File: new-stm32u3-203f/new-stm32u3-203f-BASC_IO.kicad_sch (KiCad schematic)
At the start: 0 parts

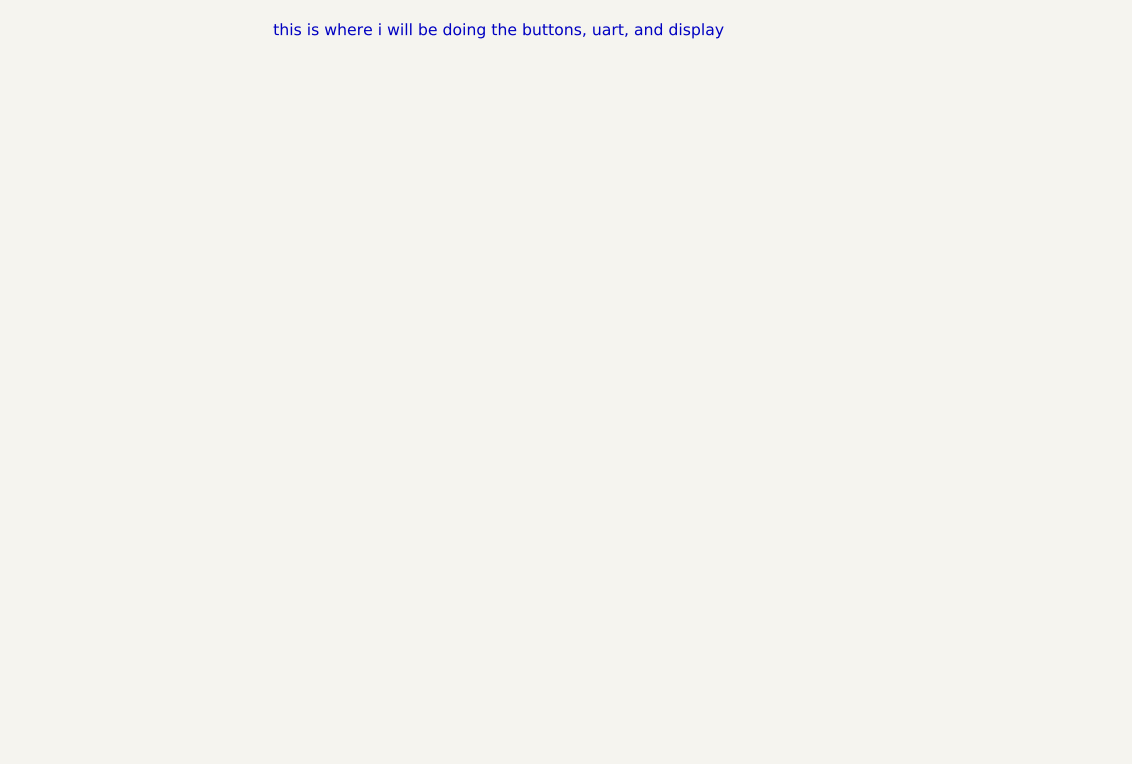
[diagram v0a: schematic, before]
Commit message: added buttons, added uart, added display.
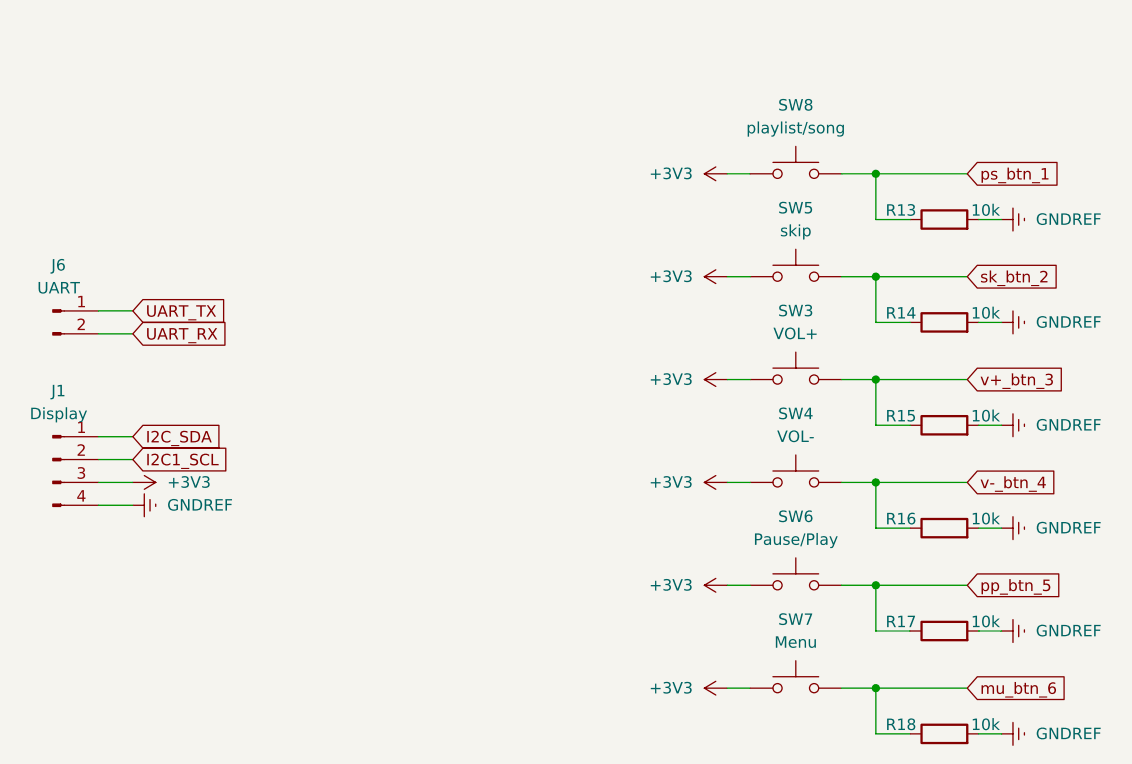
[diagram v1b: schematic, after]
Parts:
- added J1: Display, symbol Connector:Conn_01x04_Pin
- added J6: UART, symbol Connector:Conn_01x02_Pin
- added R13, R14, R15, R16, R17, R18: 10k, symbol Device:R
- added SW3: VOL+, symbol Switch:SW_Push
- added SW4: VOL-, symbol Switch:SW_Push
- added SW5: skip, symbol Switch:SW_Push
- added SW6: Pause/Play, symbol Switch:SW_Push
- added SW7: Menu, symbol Switch:SW_Push
- added SW8: playlist/song, symbol Switch:SW_Push
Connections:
- new net +3V3: J1.3 (Pin_3), SW3.1, SW4.1, SW5.1, SW6.1, SW7.1, SW8.1
- new net GNDREF: J1.4 (Pin_4), R13.2, R14.2, R15.2, R16.2, R17.2, R18.2
- new net I2C1_SCL: J1.2 (Pin_2)
- new net I2C_SDA: J1.1 (Pin_1)
- new net UART_RX: J6.2 (Pin_2)
- new net UART_TX: J6.1 (Pin_1)
- new net mu_btn_6: R18.1, SW7.2
- new net pp_btn_5: R17.1, SW6.2
- new net ps_btn_1: R13.1, SW8.2
- new net sk_btn_2: R14.1, SW5.2
- new net v+_btn_3: R15.1, SW3.2
- new net v-_btn_4: R16.1, SW4.2
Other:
- note removed: "this is where i will be doing the buttons, uart, and display"

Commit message: added reset button. asigned footprints.
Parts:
- J1: footprint (none) -> Connector_PinHeader_2.54mm:PinHeader_1x04_P2.54mm_Vertical
- J6: footprint (none) -> Connector_PinHeader_2.54mm:PinHeader_1x02_P2.54mm_Vertical
- R13, R14, R15, R16, R17, R18: footprint (none) -> Resistor_SMD:R_0603_1608Metric
- SW3, SW4, SW5, SW6, SW7, SW8: footprint (none) -> Button_Switch_SMD:Panasonic_EVQPUL_EVQPUC
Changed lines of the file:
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@@
 			)
 		)
-		(property "Footprint" ""
+		(property "Footprint" "Resistor_SMD:R_0603_1608Metric"
 			(at 149.86 42.418 90)
 			(effects
@@
 			)
 		)
-		(property "Footprint" ""
+		(property "Footprint" "Resistor_SMD:R_0603_1608Metric"
 			(at 149.86 88.138 90)
 			(effects
@@
 			)
 		)
-		(property "Footprint" ""
+		(property "Footprint" "Connector_PinHeader_2.54mm:PinHeader_1x04_P2.54mm_Vertical"
 			(at 50.8 67.31 0)
 			(effects
@@
 			)
 		)
-		(property "Footprint" ""
+		(property "Footprint" "Resistor_SMD:R_0603_1608Metric"
 			(at 149.86 53.848 90)
 			(effects
@@
 			)
 		)
-		(property "Footprint" ""
+		(property "Footprint" "Connector_PinHeader_2.54mm:PinHeader_1x02_P2.54mm_Vertical"
 			(at 50.8 50.8 0)
 			(effects
@@
 			)
 		)
-		(property "Footprint" ""
+		(property "Footprint" "Resistor_SMD:R_0603_1608Metric"
 			(at 149.86 99.568 90)
 			(effects
@@
 			)
 		)
-		(property "Footprint" ""
+		(property "Footprint" "Resistor_SMD:R_0603_1608Metric"
 			(at 149.86 65.278 90)
 			(effects
@@
 			)
 		)
-		(property "Footprint" ""
+		(property "Footprint" "Button_Switch_SMD:Panasonic_EVQPUL_EVQPUC"
 			(at 133.35 53.34 0)
 			(effects
@@
 			)
 		)
-		(property "Footprint" ""
+		(property "Footprint" "Button_Switch_SMD:Panasonic_EVQPUL_EVQPUC"
 			(at 133.35 76.2 0)
 			(effects
@@
 			)
 		)
-		(property "Footprint" ""
+		(property "Footprint" "Button_Switch_SMD:Panasonic_EVQPUL_EVQPUC"
 			(at 133.35 41.91 0)
 			(effects
@@
 			)
 		)
-		(property "Footprint" ""
+		(property "Footprint" "Resistor_SMD:R_0603_1608Metric"
 			(at 149.86 76.708 90)
 			(effects
@@
 			)
 		)
-		(property "Footprint" ""
+		(property "Footprint" "Button_Switch_SMD:Panasonic_EVQPUL_EVQPUC"
 			(at 133.35 64.77 0)
 			(effects
@@
 			)
 		)
-		(property "Footprint" ""
+		(property "Footprint" "Button_Switch_SMD:Panasonic_EVQPUL_EVQPUC"
 			(at 133.35 30.48 0)
 			(effects
@@
 			)
 		)
-		(property "Footprint" ""
+		(property "Footprint" "Button_Switch_SMD:Panasonic_EVQPUL_EVQPUC"
 			(at 133.35 87.63 0)
 			(effects

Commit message: made some progress on the pcb
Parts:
- removed R18: 10k, Resistor_SMD:R_0603_1608Metric, symbol Device:R
- removed SW7: Menu, Button_Switch_SMD:Panasonic_EVQPUL_EVQPUC, symbol Switch:SW_Push
